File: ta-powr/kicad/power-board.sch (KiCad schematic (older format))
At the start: 0 parts

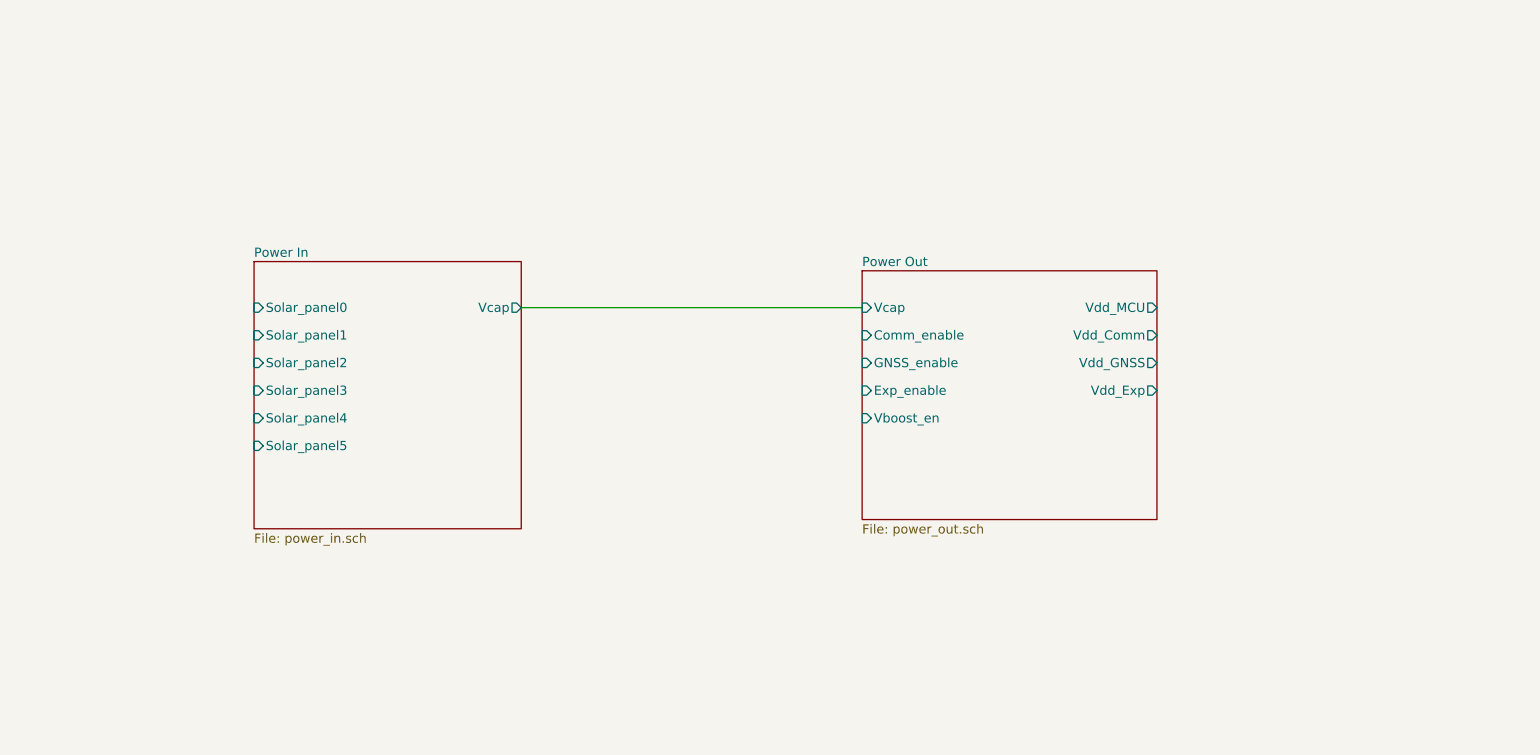
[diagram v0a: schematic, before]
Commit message: Added parts that are likely a problem
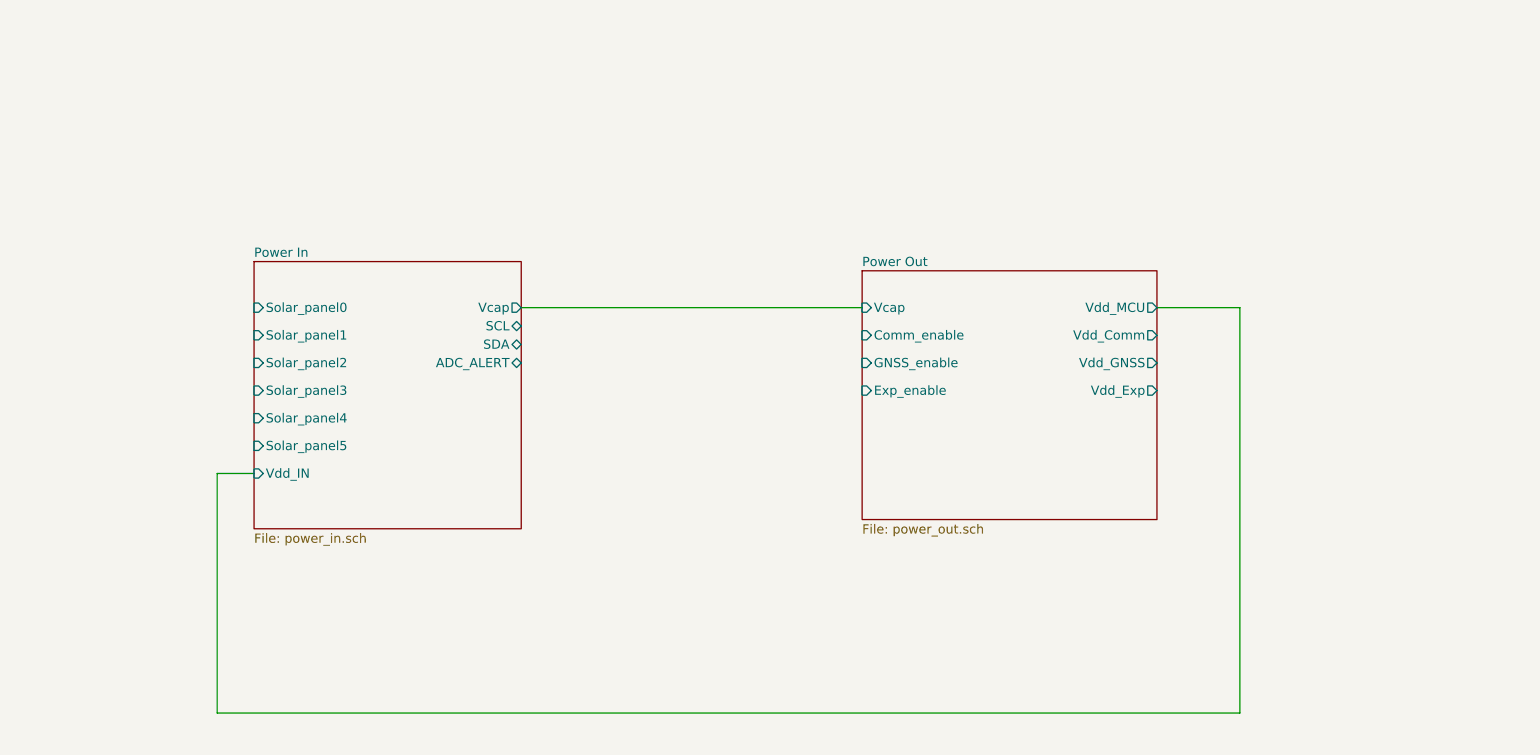
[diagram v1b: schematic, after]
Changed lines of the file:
@@
 F7 "Solar_panel5" I L 2200 3050 50
 F8 "Vcap" O R 3650 2300 50
+F9 "Vdd_IN" I L 2200 3200 50
+F10 "SCL" B R 3650 2400 50
+F11 "SDA" B R 3650 2500 50
+F12 "ADC_ALERT" B R 3650 2600 50
 $EndSheet
 $Sheet
@@
 F8 "Vdd_GNSS" O R 7100 2600 50
 F9 "Vdd_Exp" O R 7100 2750 50
-F10 "Vboost_en" I L 5500 2900 50
 $EndSheet
 Wire Wire Line
 	3650 2300 5500 2300
+Wire Wire Line
+	7100 2300 7550 2300
+Wire Wire Line
+	7550 2300 7550 4500
+Wire Wire Line
+	7550 4500 2000 4500
+Wire Wire Line
+	2000 3200 2200 3200
+Wire Wire Line
+	2000 3200 2000 4500
 $EndSCHEMATC

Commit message: added header schematic connections, added footprints to effectively every part, still need to check for bugs
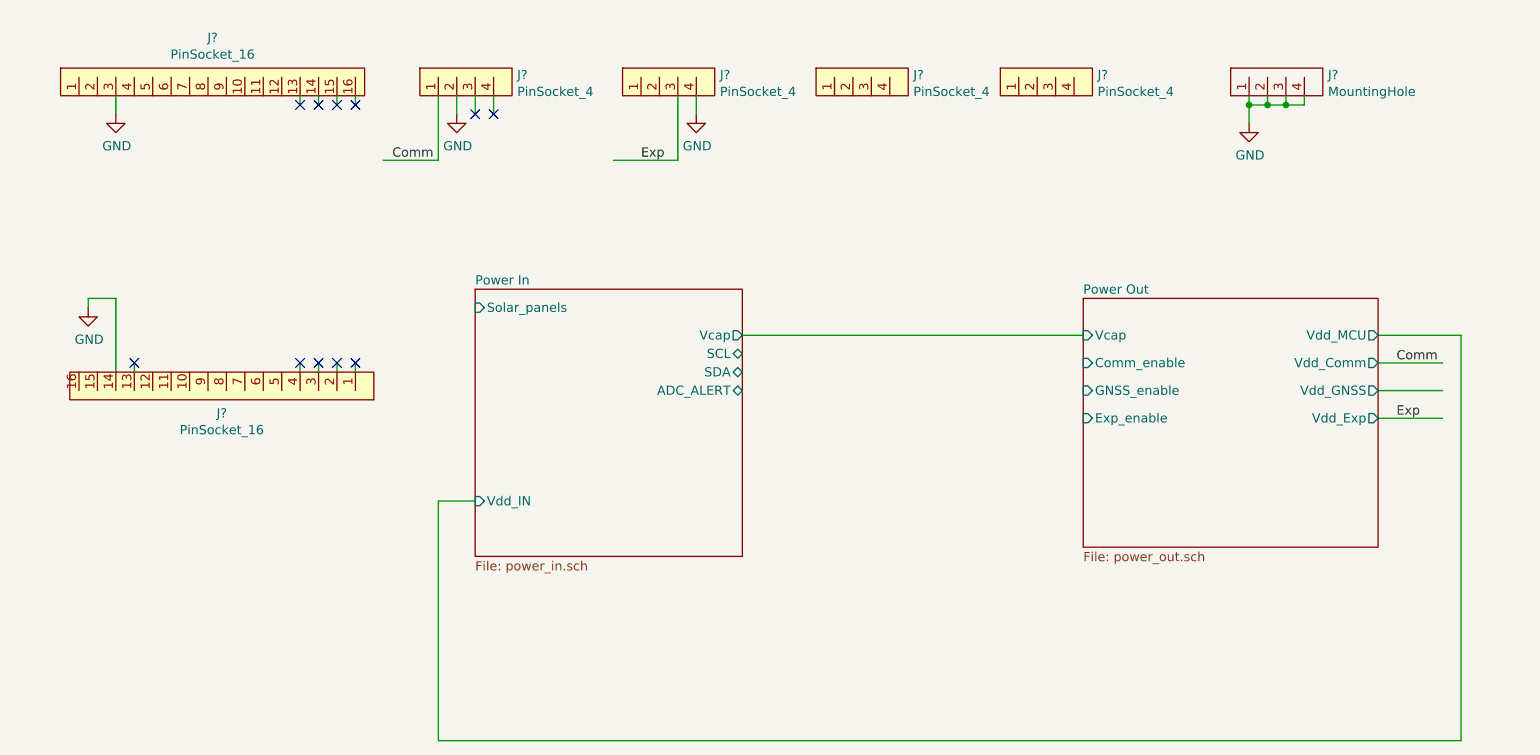
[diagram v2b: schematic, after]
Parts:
- added J? (x2): PinSocket_16, ta-powr:PinSocket_1x16_TartanArtibeus_pwr_cpy, symbol power-board:PinSocket_16
- added J? (x4): PinSocket_4, ta-powr:PinSocket_1x4_TartanArtibeus_pwr_cpy, symbol power-board:PinSocket_4
- added J?: MountingHole, ta-powr:MountingHoles_TartanArtibeus_pwr_cpy, symbol power-board:MountingHole
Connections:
- net labels added: Comm, Exp, GND
- wire segments 6 -> 38
- no-connect marks 0 -> 11

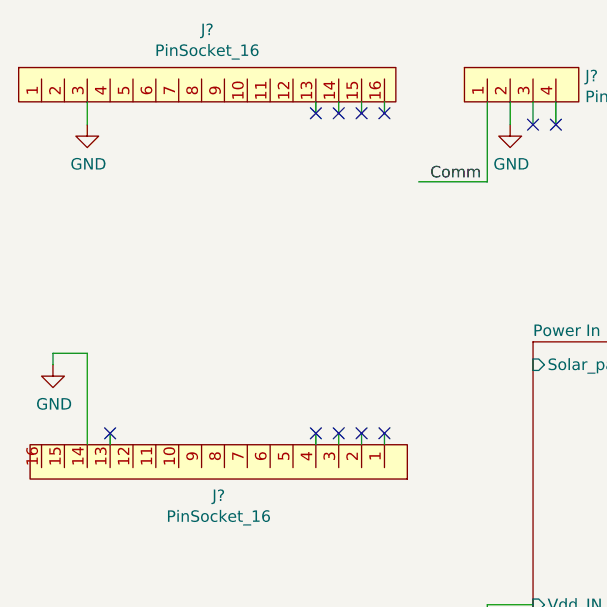
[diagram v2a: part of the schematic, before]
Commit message: tweaked header connections
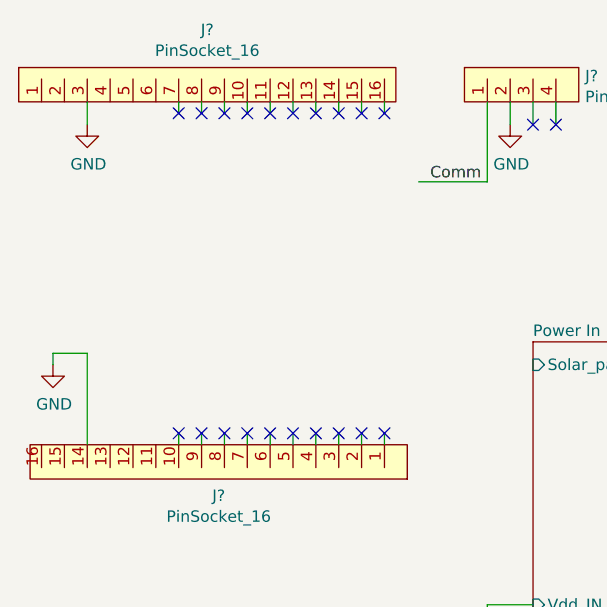
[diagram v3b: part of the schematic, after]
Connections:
- wire segments 38 -> 49
- no-connect marks 11 -> 22
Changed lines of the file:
@@
 Wire Wire Line
 	2450 2600 2450 2650
-NoConn ~ 1550 2600
-Wire Wire Line
-	1550 2600 1550 2650
 $Comp
 L power:GND #PWR?
@@
 Wire Wire Line
 	8300 2900 8650 2900
+NoConn ~ 2150 2600
+Wire Wire Line
+	2150 2600 2150 2650
+NoConn ~ 1850 1200
+NoConn ~ 1950 1200
+NoConn ~ 2050 1200
+NoConn ~ 2150 1200
+NoConn ~ 2250 1200
+NoConn ~ 2350 1200
+NoConn ~ 1850 2600
+NoConn ~ 1950 2600
+NoConn ~ 2050 2600
+NoConn ~ 2250 2600
+NoConn ~ 2350 2600
+Wire Wire Line
+	1850 2600 1850 2650
+Wire Wire Line
+	1950 2600 1950 2650
+Wire Wire Line
+	2050 2600 2050 2650
+Wire Wire Line
+	2250 2600 2250 2650
+Wire Wire Line
+	2350 2600 2350 2650
+Wire Wire Line
+	1850 1200 1850 1150
+Wire Wire Line
+	1950 1200 1950 1150
+Wire Wire Line
+	2050 1200 2050 1150
+Wire Wire Line
+	2150 1200 2150 1150
+Wire Wire Line
+	2250 1200 2250 1150
+Wire Wire Line
+	2350 1200 2350 1150
 $EndSCHEMATC

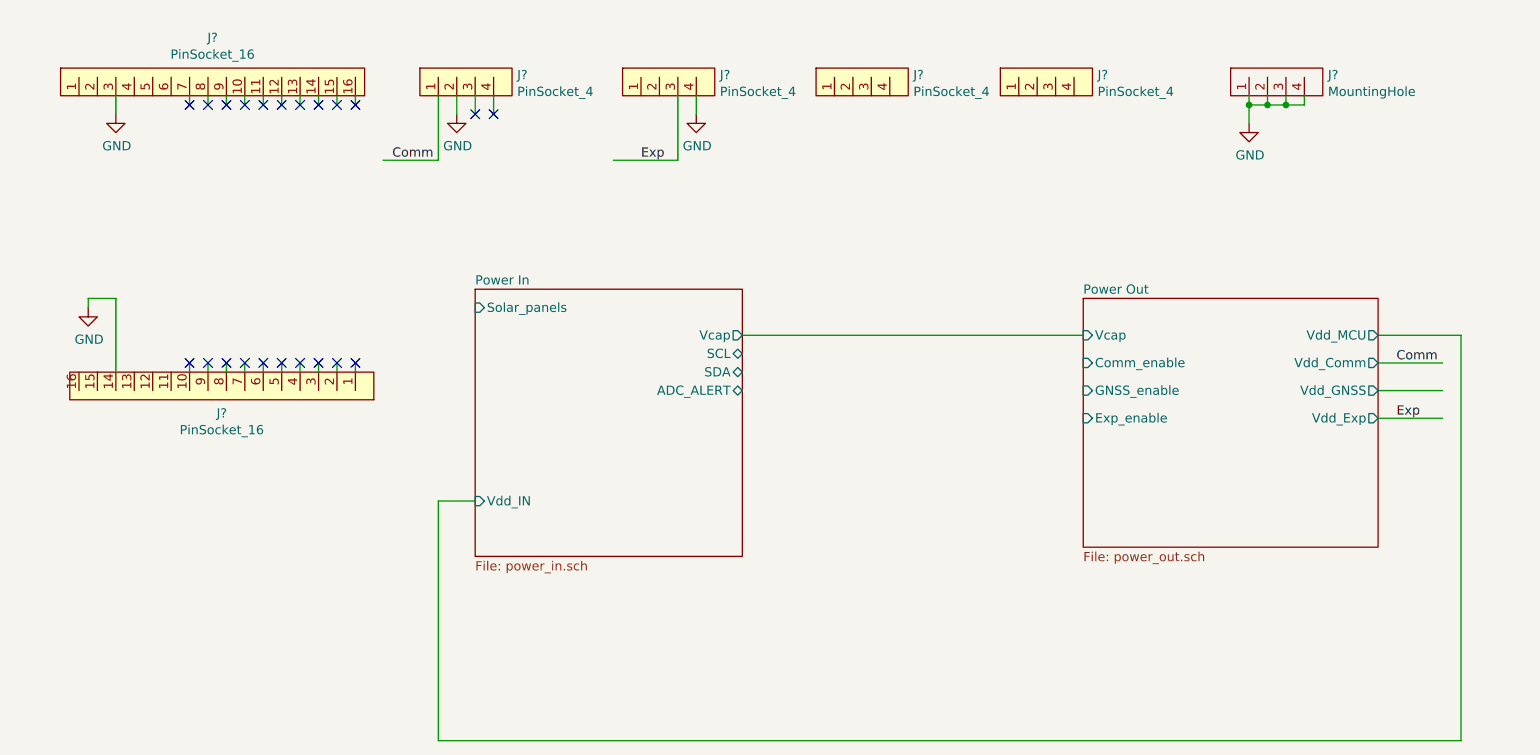
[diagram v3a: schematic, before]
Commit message: fixed electrical checker errors and generated netlist
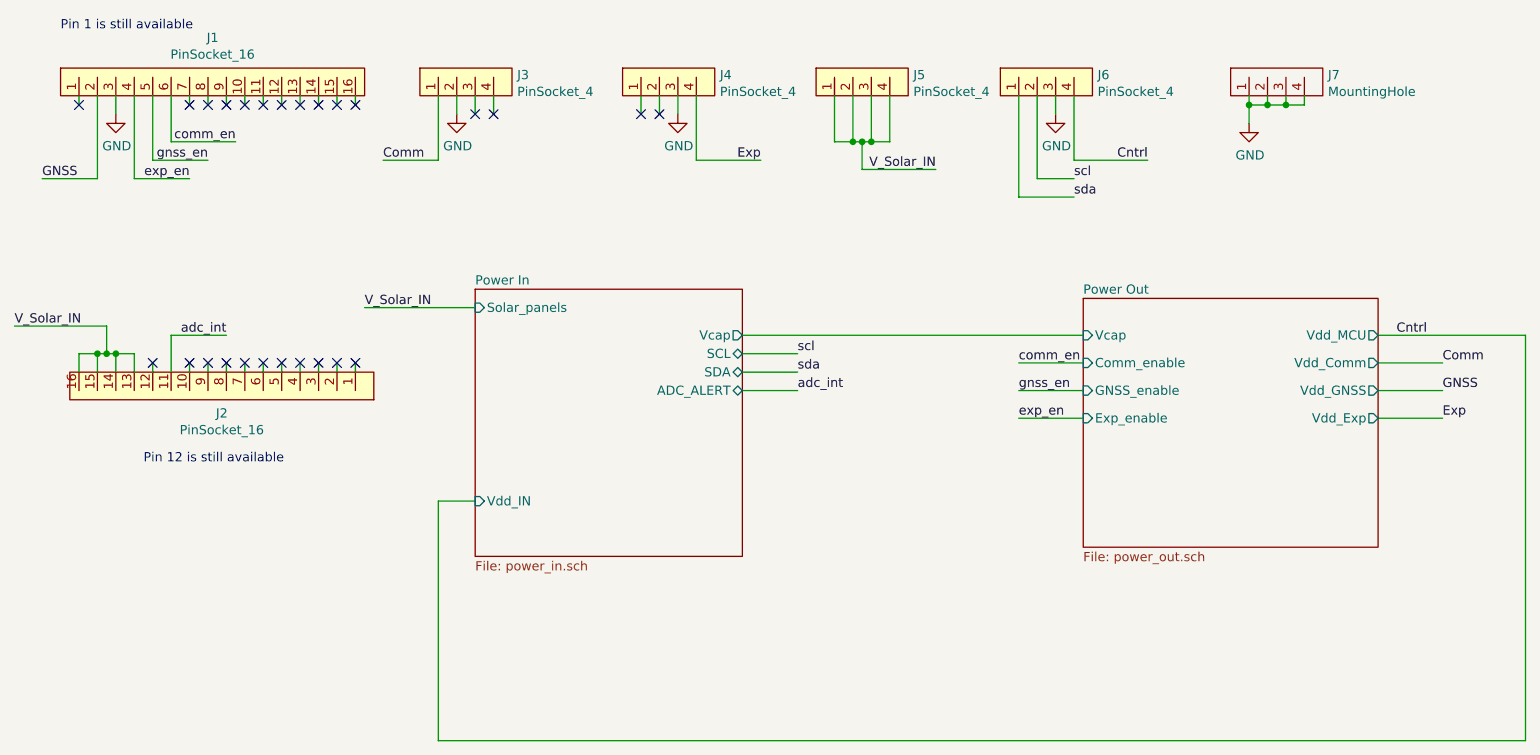
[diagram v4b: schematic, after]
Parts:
- gave numbers to parts that had none: 7
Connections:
- net labels added: Cntrl, GNSS, V_Solar_IN, adc_int, comm_en, exp_en, gnss_en, scl, sda
- wire segments 49 -> 94
- no-connect marks 22 -> 26
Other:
- note added: "Pin 1 is still available"
- note added: "Pin 12 is still available"

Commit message: first crack at parts placement on power board
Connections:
- net Cntrl: now also J1.2; no longer J6.4
- net GND: no longer J6.3
- net GNSS: now also J1.1; no longer J1.2
- net V_Solar_IN: now also J2.1, J2.2, J2.3, J2.4; no longer J2.13, J2.14, J2.15, J2.16
- net adc_int: now also J1.4; no longer J2.11
- net comm_en: now also J6.2; no longer J1.6
- net exp_en: now also J6.4; no longer J1.4
- net gnss_en: now also J6.3; no longer J1.5
- net scl: now also J1.6; no longer J6.2
- net sda: now also J1.5; no longer J6.1
- no-connect marks 26 -> 27
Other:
- note added: "Pin 5 and 6\nstill available"
- note removed: "Pin 12 is still available"
- moved on the sheet: J2
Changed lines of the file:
@@
 L power-board:PinSocket_16 J2
 U 1 1 5F0E10B5
-P 2050 2650
-F 0 "J2" H 2075 2873 50  0000 C CNN
-F 1 "PinSocket_16" H 2075 2964 50  0000 C CNN
-F 2 "ta-powr:PinSocket_1x16_TartanArtibeus_pwr_cpy" H 1650 2650 50  0001 C CNN
-F 3 "" H 1650 2650 50  0001 C CNN
-	1    2050 2650
-	-1   0    0    1
+P 1950 2650
+F 0 "J2" H 1975 2873 50  0000 C CNN
+F 1 "PinSocket_16" H 1975 2964 50  0000 C CNN
+F 2 "ta-powr:PinSocket_1x16_TartanArtibeus_pwr_cpy" H 1550 2650 50  0001 C CNN
+F 3 "" H 1550 2650 50  0001 C CNN
+	1    1950 2650
+	1    0    0    1
 $EndComp
 NoConn ~ 2750 1200
@@
 Wire Wire Line
 	6650 1500 7050 1500
-Text Label 7050 1500 2    50   ~ 0
+Text Label 1050 1600 0    50   ~ 0
 Cntrl
-$Comp
-L power:GND #PWR?
-U 1 1 5F0F8F68
-P 6550 1250
-AR Path="/5EF1389E/5F0F8F68" Ref="#PWR?"  Part="1"
-AR Path="/5F0F8F68" Ref="#PWR0112"  Part="1"
-F 0 "#PWR0112" H 6550 1000 50  0001 C CNN
-F 1 "GND" H 6555 1077 50  0000 C CNN
-F 2 "" H 6550 1250 50  0001 C CNN
-F 3 "" H 6550 1250 50  0001 C CNN
-	1    6550 1250
-	1    0    0    -1
-$EndComp
-Wire Wire Line
-	6550 1150 6550 1250
 Wire Wire Line
 	4850 2550 5150 2550
@@
 Text Label 5150 2650 0    50   ~ 0
 sda
-Wire Wire Line
-	6350 1150 6350 1700
-Wire Wire Line
-	6350 1700 6650 1700
-Wire Wire Line
-	6450 1150 6450 1600
-Wire Wire Line
-	6450 1600 6650 1600
-Text Label 6650 1600 0    50   ~ 0
+Text Label 2100 1400 2    50   ~ 0
 scl
-Text Label 6650 1700 0    50   ~ 0
+Text Label 1950 1500 2    50   ~ 0
 sda
 Wire Wire Line
@@
 Wire Wire Line
 	1550 1150 1550 1600
-Wire Wire Line
-	1750 2650 1750 2450
-Wire Wire Line
-	1750 2450 2050 2450
-Text Label 2050 2450 2    50   ~ 0
+Text Label 1850 1600 2    50   ~ 0
 adc_int
-Text Label 2100 1400 2    50   ~ 0
+Text Label 6900 1700 2    50   ~ 0
 comm_en
 Wire Wire Line
 	1750 1400 2100 1400
-Text Label 1950 1500 2    50   ~ 0
+Text Label 7000 1600 2    50   ~ 0
 gnss_en
-Text Label 1850 1600 2    50   ~ 0
+Text Label 7050 1500 2    50   ~ 0
 exp_en
 Wire Wire Line
 	1550 1600 1850 1600
-Text Label 1050 1600 0    50   ~ 0
+Text Label 1000 1500 0    50   ~ 0
 GNSS
 $Comp
@@
 	1350 1600 1050 1600
 NoConn ~ 1650 2600
-NoConn ~ 1250 1200
-Wire Wire Line
-	1250 1150 1250 1200
 Wire Wire Line
 	1650 2600 1650 2650
-Text Notes 1600 3150 0    50   ~ 0
-Pin 12 is still available
-Text Notes 1150 800  0    50   ~ 0
+Text Notes 1550 3250 0    50   ~ 0
+Pin 5 and 6\nstill available
+Text Notes 6300 950  0    50   ~ 0
 Pin 1 is still available
+Wire Wire Line
+	1250 1500 1000 1500
+Wire Wire Line
+	1250 1150 1250 1500
+Wire Wire Line
+	6550 1150 6550 1600
+Wire Wire Line
+	6450 1700 6900 1700
+Wire Wire Line
+	6450 1150 6450 1700
+Wire Wire Line
+	6550 1600 7000 1600
+NoConn ~ 6350 1200
+Wire Wire Line
+	6350 1150 6350 1200
+NoConn ~ 1750 2600
+Wire Wire Line
+	1750 2600 1750 2650
 $EndSCHEMATC
